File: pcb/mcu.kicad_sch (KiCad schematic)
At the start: 24 parts, among them J2 AVR-UPDI-UART-6, U4 ATtiny1616-MNR

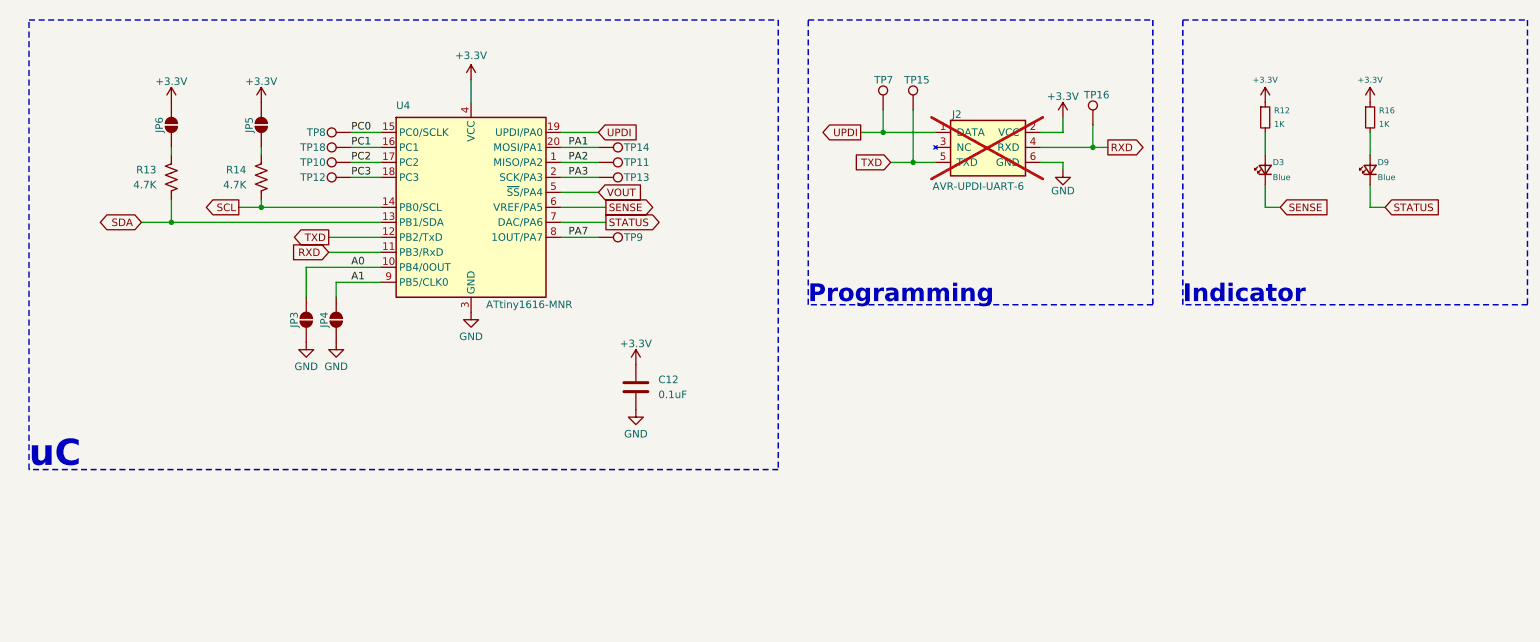
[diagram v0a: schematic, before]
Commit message: refactored to STM32
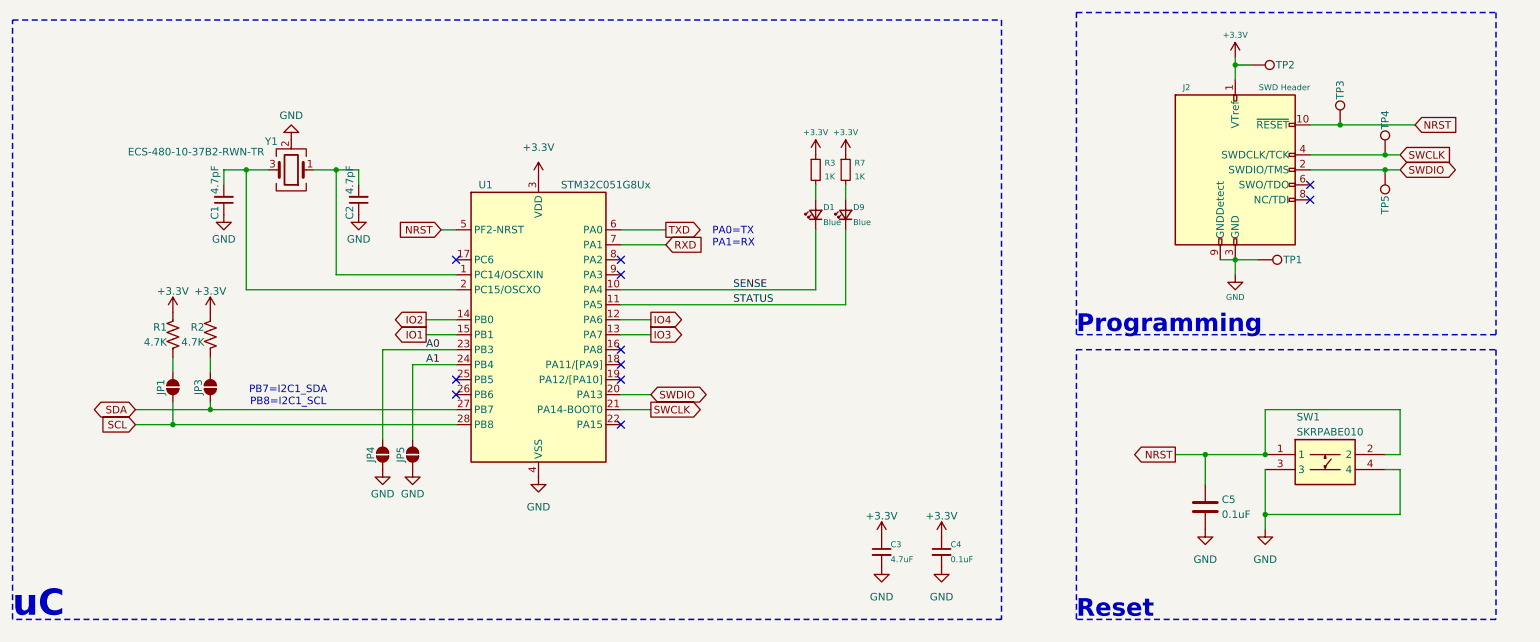
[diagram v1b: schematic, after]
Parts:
- removed C12: 0.1uF, CRGM Passive:C_0603_1608Metric, symbol Device:C
- removed D3, D9: Blue, CRGM Passive:LED_0603_1608Metric, symbol Device:LED_Small
- removed J2: AVR-UPDI-UART-6, CRGM Connector:PinHeader_2x03_P2.54mm_Vertical_SMD, symbol CRGM Connector:AVR-UPDI-UART-6
- removed JP3, JP4: ~, CRGM Connector:SolderJumper-2_P1.3mm_Open_RoundedPad1.0x1.5mm, symbol Jumper:SolderJumper_2_Open
- removed JP6: ~, CRGM Connector:SolderJumper-2_P1.3mm_Open_RoundedPad1.0x1.5mm, symbol CRGM Connector:SolderJumper_2_Open
- removed R13, R14: 4.7K, CRGM Passive:R_0603_1608Metric, symbol Device:R_US
- removed R16: 1K, CRGM Passive:R_0603_1608Metric, symbol Device:R_Small
- removed TP10, TP11, TP12, TP13, TP14, TP15, TP16, TP18, TP7, TP8, TP9: ~, CRGM Mechanical:TestPoint_Pad_D1.0mm, symbol CRGM Connector:TestPoint
- removed U4: ATtiny1616-MNR, CRG Makes:VQFN-20-1EP_3x3mm_P0.4mm_EP1.7x1.7mm_ThermalVias, symbol CRG Makes:ATtiny1616-MNR
- added C1, C2: 4.7pF, CRGM Passive:C_0603_1608Metric, symbol CRGM Passive:C_Small
- added C3: 4.7uF, CRGM Passive:C_0603_1608Metric, symbol Device:C_Small
- added C4: 0.1uF, CRGM Passive:C_0603_1608Metric, symbol Device:C_Small
- added C5: 0.1uF, CRGM Passive:C_0603_1608Metric, symbol Device:C
- added D1, D9: Blue, CRGM Passive:LED_0603_1608Metric, symbol CRGM Passive:LED_Small
- added J2: SWD Header, CRGM Connector:PinHeader_2x05_P1.27mm_Vertical_SMD, symbol Connector:Conn_ARM_JTAG_SWD_10
- added JP1, JP3, JP4: SolderJumper_2_Open, CRGM Connector:SolderJumper-2_P1.3mm_Open_RoundedPad1.0x1.5mm, symbol CRGM Connector:SolderJumper_2_Open
- added R1, R2: 4.7K, CRGM Passive:R_0603_1608Metric, symbol Device:R_US
- added R7: 1K, CRGM Passive:R_0603_1608Metric, symbol Device:R_Small
- added SW1: SKRPABE010, CRGM Switches:SMD-4P-4.2x3.2mm, symbol CRGM Switches:SKRPABE010
- added TP1, TP2, TP3, TP4, TP5: (no value), CRGM Mechanical:TestPoint_Pad_D1.0mm, symbol Connector:TestPoint
- added U1: STM32C051G8Ux, CRG Makes:QFN-28_4x4mm_P0.5mm, symbol CRG Makes:STM32C051G8Ux
- added Y1: ECS-480-10-37B2-RWN-TR, CRGM Passive:Crystal_SMD_2016-4Pin_2.0x1.6mm, symbol CRGM Passive:ECS-480-10-37B2-RWN-TR
- JP5: value ~ -> SolderJumper_2_Open
- renumbered R12 to R3
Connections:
- net +3.3V: now also C3.1, C4.1, J2.1 (VTref), R1.2, R2.2, R7.1, TP2.1, U1.3 (VDD); no longer JP5.2 (B)
- net A0: now also JP4.2 (B), U1.23 (PB3)
- net A1: now also JP5.2 (B), U1.24 (PB4)
- net GND: now also JP5.1 (A), C1.1, C2.1, C3.2, C4.2, C5.2, J2.3 (GND), J2.5 (GND), J2.9 (GNDDetect), JP4.1 (A), SW1.3, SW1.4, TP1.1, U1.4 (VSS), Y1.2 (G), Y1.4 (G)
- net RXD: now also U1.7 (PA1)
- net SCL: now also JP1.1 (A), U1.28 (PB8)
- net SDA: now also JP3.1 (A), U1.27 (PB7)
- net SENSE: now also D1.1 (K), U1.10 (PA4)
- net STATUS: now also D9.1 (K), U1.11 (PA5)
- net TXD: now also U1.6 (PA0)
- net at R3.2: now also D1.2 (A)
- new net: JP3.2 (B), R2.1
- new net: JP1.2 (B), R1.1
- new net: C2.2, U1.1 (PC14/OSCXIN), Y1.1
- new net: C1.2, U1.2 (PC15/OSCXO), Y1.3
- new net: D9.2 (A), R7.2
- new net IO1: U1.15 (PB1)
- new net IO2: U1.14 (PB0)
- new net IO3: U1.13 (PA7)
- new net IO4: U1.12 (PA6)
- new net NRST: C5.1, J2.10 (~{RESET}), SW1.1, SW1.2, TP3.1, U1.5 (PF2-NRST)
- new net SWCLK: J2.4 (SWDCLK/TCK), TP4.1, U1.21 (PA14-BOOT0)
- new net SWDIO: J2.2 (SWDIO/TMS), TP5.1, U1.20 (PA13)
- no-connect marks 0 -> 11
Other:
- note added: "PA0=TX PA1=RX"
- note added: "PB7=I2C1_SDA PB8=I2C1_SCL"
- note added: "Reset"
- note removed: "Indicator"
- moved on the sheet: R3

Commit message: Added additional silkscreen to AC side
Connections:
- net IO1: now also U1.10 (PA4); no longer U1.15 (PB1)
- net IO2: now also U1.11 (PA5); no longer U1.14 (PB0)
- net IO3: now also U1.12 (PA6); no longer U1.13 (PA7)
- net IO4: now also U1.13 (PA7); no longer U1.12 (PA6)
- net SENSE: now also U1.14 (PB0); no longer U1.10 (PA4)
- net STATUS: now also U1.15 (PB1); no longer U1.11 (PA5)
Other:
- moved on the sheet: C1, C2, C3, C4, D1, D9, R3, R7, Y1

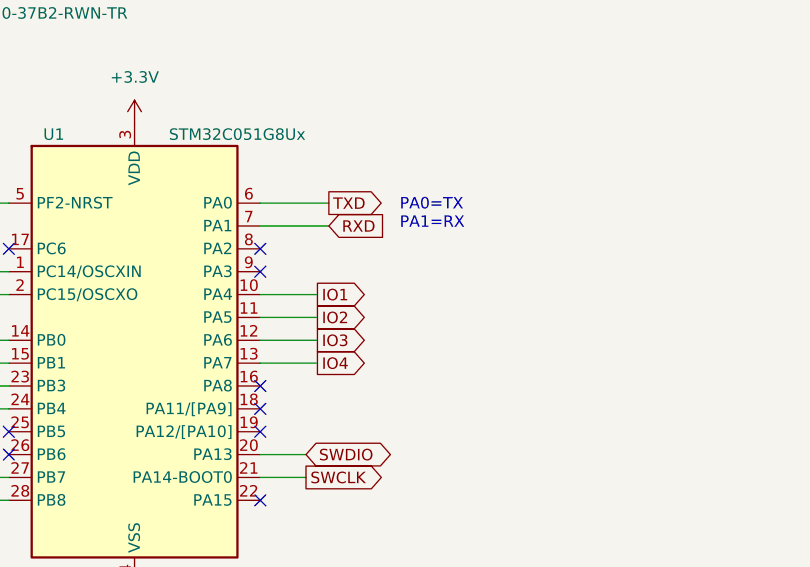
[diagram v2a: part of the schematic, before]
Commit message: Removed AC input via copper
Testing revealed sending AC through copper did not trigger device. Removed ability to send AC through the PCB.
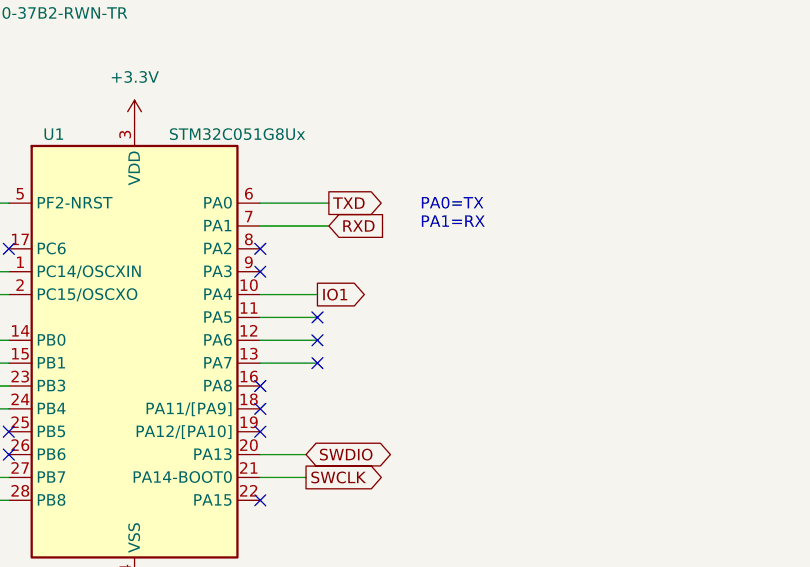
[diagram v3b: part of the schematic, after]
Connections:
- net IO2: no longer names the net of U1.11 (PA5)
- net IO3: no longer names the net of U1.12 (PA6)
- net IO4: no longer names the net of U1.13 (PA7)
- no-connect marks 11 -> 14
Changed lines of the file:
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@@
 	(text "PA0=TX\nPA1=RX"
 		(exclude_from_sim no)
-		(at 141.224 62.23 0)
+		(at 143.51 62.23 0)
 		(effects
 			(font
@@
 	)
 	(no_connect
+		(at 132.08 78.74)
+	)
+	(no_connect
 		(at 97.79 88.9)
 	)
 	(no_connect
+		(at 132.08 73.66)
+	)
+	(no_connect
 		(at 97.79 86.36)
+	)
+	(no_connect
+		(at 132.08 76.2)
 	)
 	(no_connect
@@
 		)
 	)
-	(global_label "IO3"
-		(shape output)
-		(at 132.08 76.2 0)
-		(fields_autoplaced yes)
-		(effects
-			(font
-				(size 1.27 1.27)
-			)
-			(justify left)
-		)
-		(property "Intersheetrefs" "${INTERSHEET_REFS}"
-			(at 138.21 76.2 0)
-			(show_name no)
-			(do_not_autoplace no)
-			(effects
-				(font
-					(size 1.27 1.27)
-				)
-				(justify left)
-			)
-		)
-	)
 	(global_label "SWCLK"
 		(shape input)
@@
 			)
 		)
-	)
-	(global_label "IO4"
-		(shape output)
-		(at 132.08 78.74 0)
-		(fields_autoplaced yes)
-		(effects
-			(font
-				(size 1.27 1.27)
-			)
-			(justify left)
-		)
-		(property "Intersheetrefs" "${INTERSHEET_REFS}"
-			(at 138.21 78.74 0)
-			(show_name no)
-			(do_not_autoplace no)
-			(effects
-				(font
-					(size 1.27 1.27)
-				)
-				(justify left)
-			)
-		)
-	)
-	(global_label "IO2"
-		(shape output)
-		(at 132.08 73.66 0)
-		(fields_autoplaced yes)
-		(effects
-			(font
-				(size 1.27 1.27)
-			)
-			(justify left)
-		)
-		(property "Intersheetrefs" "${INTERSHEET_REFS}"
-			(at 138.21 73.66 0)
-			(show_name no)
-			(do_not_autoplace no)
-			(effects
-				(font
-					(size 1.27 1.27)
-				)
-				(justify left)
-			)
-		)

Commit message: Added alternative part numbers for LCSC
Moved silkscreen a little
Updated requirements to indicate 1oz cu vs 2oz.
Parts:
- C1, C2: LCSC1 (none) -> C282071
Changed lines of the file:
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@@
+			)
+		)
+		(property "LCSC1" "C282071"
+			(at 90.17 48.26 90)
+			(hide yes)
+			(show_name no)
+			(do_not_autoplace no)
+			(effects
+				(font
+					(size 1.27 1.27)
+				)
 			)
 		)
@@
 			(at 67.31 48.26 90)
 			(hide yes)
+			(show_name no)
+			(do_not_autoplace no)
+			(effects
+				(font
+					(size 1.27 1.27)
+				)
+			)
+		)
+		(property "LCSC1" "C282071"
+			(at 67.31 48.26 90)
+			(hide yes)
